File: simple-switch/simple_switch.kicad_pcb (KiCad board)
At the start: 2 copper layers, 28.6 x 27.9 mm, 23 parts, among them J1 CON_TERM_BLK_1X2_TB008A-508-0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, J2 CON_HDR_100MILS_M_TH_2X8, J3 CON_HDR_100MILS_M_TH_1X2, Q1 TRX_PMOS_AOD4189, Q2 TRX_2NPN_BC846S,115

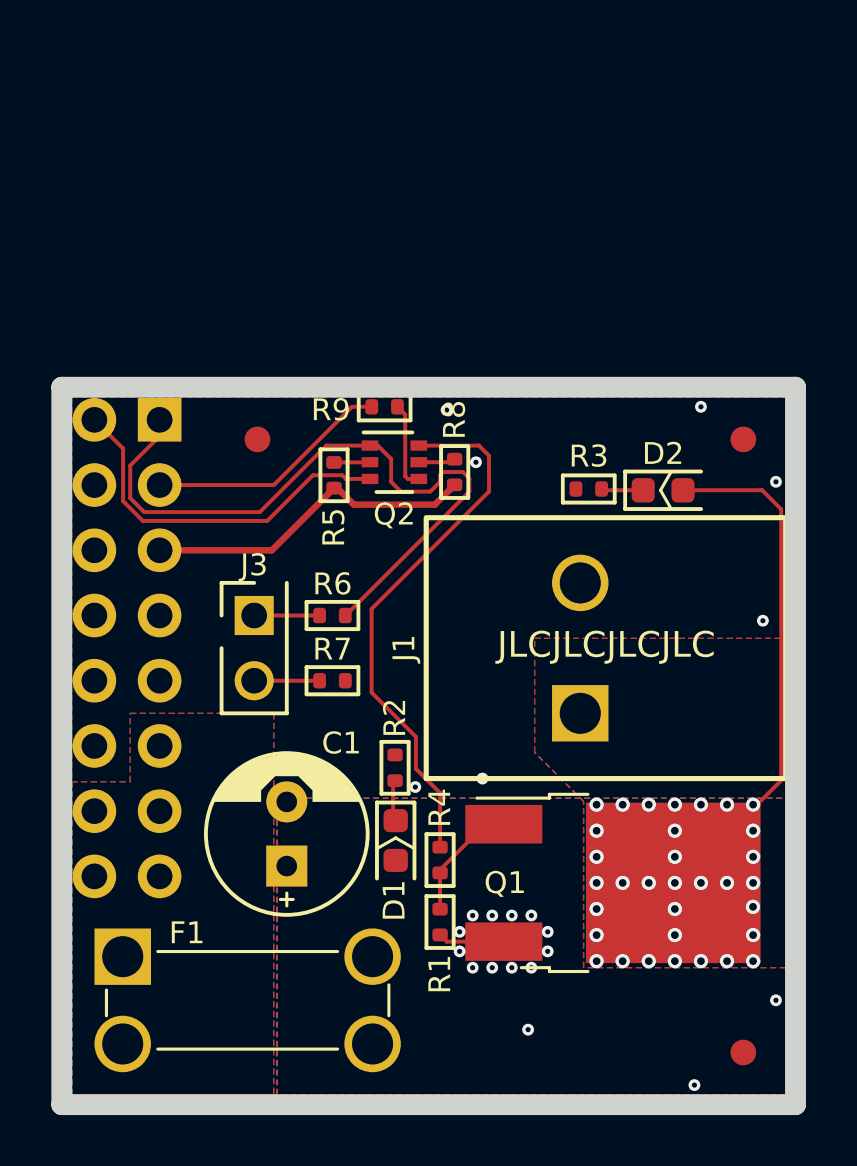
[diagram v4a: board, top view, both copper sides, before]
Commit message: Invert connectors (male/female) Replace TH connectors with SMD ones on mainboard Add 555 timer on simple-switch to generate 60 Hz Add jumper on simple-switch to select AC Add series I2C resistors on mainboard from mikroBUS socket
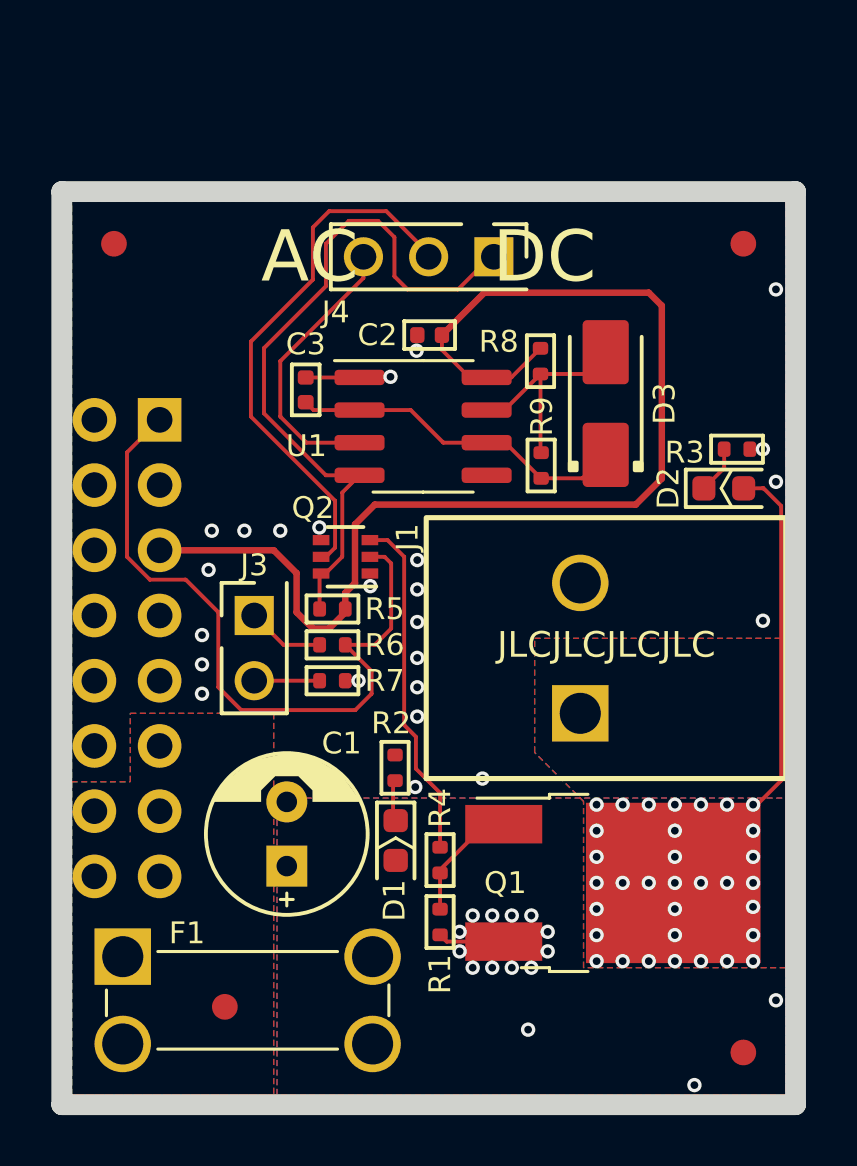
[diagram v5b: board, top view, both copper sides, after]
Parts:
- added C2: CAP_CER_100NF_25V_0402, connaxio-capacitors:CAP_CER_0402_1005M, F.Cu at (128.2, 58.9)
- added C3: CAP_CER_100NF_25V_0402, connaxio-capacitors:CAP_CER_0402_1005M, F.Cu at (123.4, 61.1)
- added D3: DIO_SBD_100V_3A_SMA, connaxio-diodes:DO-214AC_SMA, F.Cu at (135.1, 61.6)
- added F2: FID_1X1, connaxio-mechanical:FID_1X1, F.Cu at (120.3, 85.1)
- added J4: CON_HDR_100MILS_M_TH_1X3, connaxio-connectors:CON_HDR_100MILS_M_TH_1X3, F.Cu at (128.2, 55.9)
- added U1: TIMER_TLC555IDR, connaxio-sop:SOIC-8_3.9x4.9_P1.27, F.Cu at (128.0, 62.5)
- J2: value CON_HDR_100MILS_M_TH_2X8 -> CON_HDR_100MILS_F_TH_2X8; footprint connaxio-connectors:CON_HDR_100MILS_M_TH_2X8 -> connaxio-connectors:CON_HDR_100MILS_F_TH_2X8
- R8: value RES_12.4KΩ_1%_0402 -> RES_100KΩ_1%_0402
- R9: value RES_226Ω_1%_0402 -> RES_169KΩ_1%_0402
- moved F3 9.45 mm to (116.0, 55.4)
- moved F4 7.62 mm to (140.5, 55.4)
- moved R9 6.51 mm to (132.6, 64.0), turned to -90 degrees
- moved R3 5.98 mm to (140.2, 63.4), turned to 0 degrees
- moved R8 5.46 mm to (132.6, 59.9), turned to -90 degrees
- moved R5 5.21 mm to (124.5, 69.6), turned to 180 degrees
- moved G*** 4.57 mm to (132.1, 58.8)
- moved G*** 4.20 mm to (138.8, 64.1)
- moved Q2 4.15 mm to (125.0, 67.6), turned to 180 degrees
- moved D2 2.36 mm to (139.7, 64.9)
- moved R6 1.14 mm to (124.5, 71.0)
- renumbered F2 to F3, F3 to F4, F4 to F5
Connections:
- net Net-(F1-Pad1) renamed /VDR_IN
- J2 pad 2: /~{FAULT} -> unconnected-(J2-Pad2)
- J2 pad 3: /~{CTRLB} -> unconnected-(J2-Pad3)
- Q2 pad 1: /~{CTRLA} -> GND
- Q2 pad 2: Net-(Q2-Pad2) -> /~{CTRLA}
- Q2 pad 3: /~{FAULT} -> /PMOS_GATE
- Q2 pad 4: Net-(Q2-Pad4) -> GND
- Q2 pad 5: Net-(Q2-Pad5) -> /PMOS_CTRL
- Q2 pad 6: /PMOS_CTRL -> /CTRLA_POS
- R4 pad 2: /PMOS_CTRL -> /PMOS_GATE
- R5 pad 2: Net-(Q2-Pad2) -> /CTRLA_POS
- R8 pad 2: Net-(Q2-Pad5) -> Net-(D3-Pad2)
- R9 pad 1: /~{CTRLB} -> Net-(D3-Pad2)
- R9 pad 2: Net-(Q2-Pad4) -> Net-(C3-Pad1)
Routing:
- net +3.3V: track 13.1 -> 47.4 mm
- net /CTRLA_POS: track 0.00 -> 27.8 mm
- net /~{FAULT}: track 14.4 -> 0.00 mm
- net /PMOS_GATE: track 0.00 -> 13.5 mm
- net Net-(C3-Pad1): track 0.00 -> 12.6 mm
- net /AC_OUT: track 0.00 -> 11.2 mm
- net /~{CTRLB}: track 9.53 -> 0.00 mm
- net Net-(D3-Pad2): track 0.00 -> 8.65 mm
- net Net-(Q2-Pad4): track 3.40 -> 0.00 mm
- net /VOUT: track 20.5 -> 18.3 mm
- net GND: track 0.00 -> 2.10 mm, vias 7 -> 24
- net Net-(Q2-Pad5): track 1.45 -> 0.00 mm
- net Net-(Q2-Pad2): track 1.41 -> 0.00 mm
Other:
- board size 28.6 x 27.9 mm -> 28.6 x 35.6 mm
- board text added: "AC DC"

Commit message: Add flyback diode to simple-switch
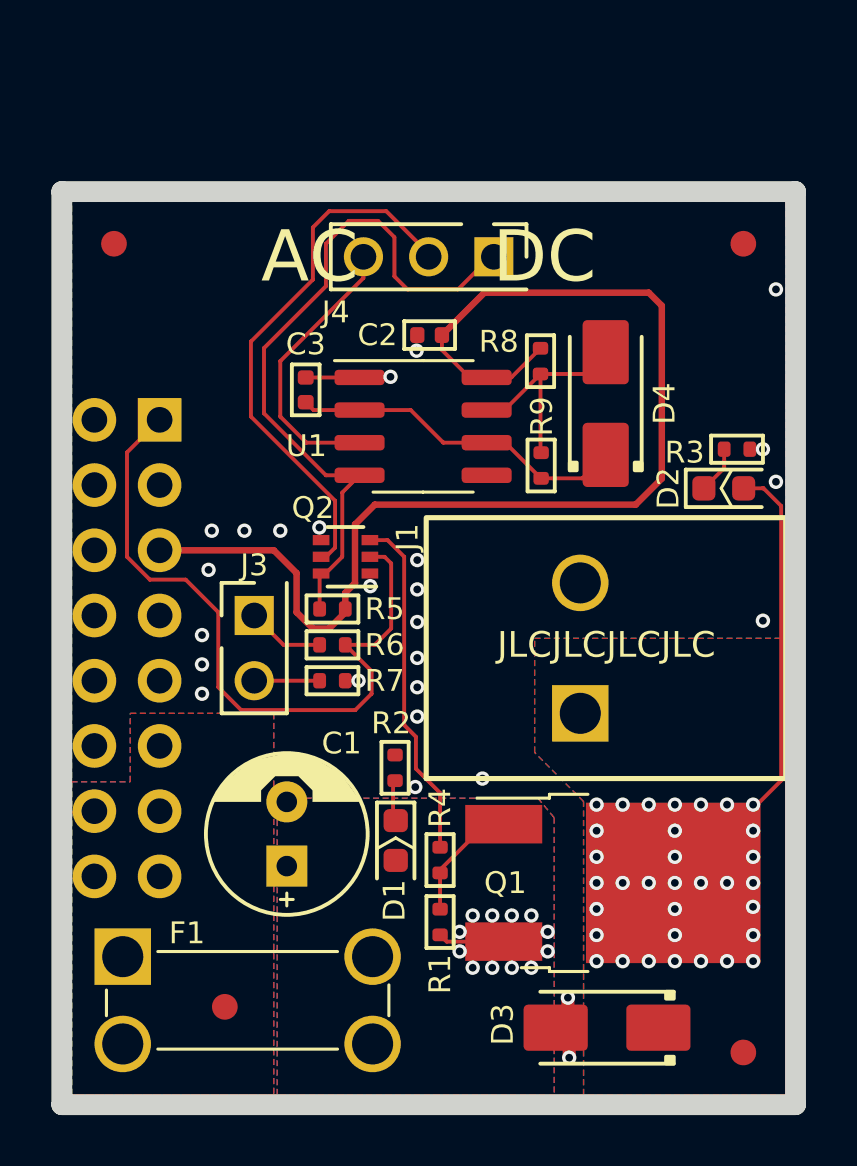
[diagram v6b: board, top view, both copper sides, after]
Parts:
- added D3: DIO_SBD_100V_3A_SMA, connaxio-diodes:DO-214AC_SMA, F.Cu at (135.2, 85.9)
- renumbered D3 to D4
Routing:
- net GND: track 2.10 -> 4.85 mm, vias 24 -> 26
- net Vdrive: vias 15 -> 12
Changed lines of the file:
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@@
   (net 9 "Net-(J3-Pad1)")
   (net 10 "Net-(J3-Pad2)")
-  (net 11 "Net-(D3-Pad2)")
+  (net 11 "Net-(D4-Pad2)")
   (net 12 "unconnected-(J2-Pad4)")
   (net 13 "unconnected-(J2-Pad2)")
@@
     )
   )
+  (footprint "connaxio-diodes:DO-214AC_SMA" (layer "F.Cu")
+    (at 135.1534 85.9028 180)
+    (descr "Diode SMA (DO-214AC)")
+    (tags "Diode SMA (DO-214AC)")
+    (property "Current" "3A")
+    (property "Manufacturer" "Micro Commercial Co")
+    (property "Manufacturer Part Number" "SL310A-TP")
+    (property "Package" "SMA")
+    (property "Polarized" "Yes")
+    (property "Sheetfile" "simple_switch.kicad_sch")
+    (property "Sheetname" "")
+    (property "Temperature" "-55°C to +150°C")
+    (property "Tolerance" "60A")
+    (property "Voltage" "100V")
+    (solder_mask_margin 0.05)
+    (attr smd)
+    (fp_text reference "D3" (at 4.064 0.127 90) (layer "F.SilkS")
+      (effects (font (size 0.85 0.85) (thickness 0.15)))
+    )
+    (fp_text value "DIO_SBD_100V_3A_SMA" (at 0 2.6) (layer "F.Fab")
+      (effects (font (size 1 1) (thickness 0.15)))
+    )
+    (fp_text user "${REFERENCE}" (at 0 -2.5) (layer "F.Fab")
+      (effects (font (size 1 1) (thickness 0.15)))
+    )
+    (fp_line (start -2.6 -1.4) (end 2.6 -1.4) (layer "F.SilkS") (width 0.15))
+    (fp_line (start -2.6 1.4) (end 2.6 1.4) (layer "F.SilkS") (width 0.15))
+    (fp_poly (pts
+        (xy -2.3 -1.13)
+        (xy -2.6 -1.13)
+        (xy -2.6 -1.4)
+        (xy -2.3 -1.4)
+      ) (layer "F.SilkS") (width 0.15) (fill solid))
+    (fp_poly (pts
+        (xy -2.3 1.4)
+        (xy -2.6 1.4)
+        (xy -2.6 1.13)
+        (xy -2.3 1.13)
+      ) (layer "F.SilkS") (width 0.15) (fill solid))
+    (fp_line (start -3.5 -1.75) (end 3.5 -1.75) (layer "F.CrtYd") (width 0.05))
+    (fp_line (start -3.5 1.75) (end -3.5 -1.75) (layer "F.CrtYd") (width 0.05))
+    (fp_line (start 3.5 -1.75) (end 3.5 1.75) (layer "F.CrtYd") (width 0.05))
+    (fp_line (start 3.5 1.75) (end -3.5 1.75) (layer "F.CrtYd") (width 0.05))
+    (fp_line (start -2.3 1.5) (end -2.3 -1.5) (layer "F.Fab") (width 0.1))
+    (fp_line (start -0.64944 0.00102) (end 0.50118 -0.79908) (layer "F.Fab") (width 0.1))
+    (fp_line (start -0.64944 -0.79908) (end -0.64944 0.80112) (layer "F.Fab") (width 0.1))
+    (fp_line (start -0.64944 0.00102) (end -1.55114 0.00102) (layer "F.Fab") (width 0.1))
+    (fp_line (start 2.3 1.5) (end -2.3 1.5) (layer "F.Fab") (width 0.1))
+    (fp_line (start -0.64944 0.00102) (end 0.50118 0.75032) (layer "F.Fab") (width 0.1))
+    (fp_line (start 0.50118 0.00102) (end 1.4994 0.00102) (layer "F.Fab") (width 0.1))
+    (fp_line (start 0.50118 0.75032) (end 0.50118 -0.79908) (layer "F.Fab") (width 0.1))
+    (fp_line (start 2.3 -1.5) (end -2.3 -1.5) (layer "F.Fab") (width 0.1))
+    (fp_line (start 2.3 -1.5) (end 2.3 1.5) (layer "F.Fab") (width 0.1))
+    (pad "1" smd roundrect (at -2 0 180) (size 2.5 1.8) (layers "F.Cu" "F.Paste" "F.Mask") (roundrect_rratio 0.1)
+      (net 18 "/VOUT") (pinfunction "K") (pintype "passive"))
+    (pad "2" smd roundrect (at 2 0 180) (size 2.5 1.8) (layers "F.Cu" "F.Paste" "F.Mask") (roundrect_rratio 0.1)
+      (net 2 "GND") (pinfunction "A") (pintype "passive"))
+    (model ":CONNAXIO_KICAD_LIB_DIR:connaxio-diodes.3dshapes/DO-214AC_SMA.wrl"
+      (offset (xyz 0 0 0))
+      (scale (xyz 1 1 1))
+      (rotate (xyz 0 0 0))
+    )
+  )
   (footprint "connaxio-diodes:LED_0603_1608M" (layer "F.Cu")
     (at 126.9238 78.613 -90)
@@
       (net 1 "+3.3V") (pinfunction "1") (pintype "passive"))
     (pad "2" smd roundrect (at 0.5 0 270) (size 0.5 0.6) (layers "F.Cu" "F.Paste" "F.Mask") (roundrect_rratio 0.25)
-      (net 11 "Net-(D3-Pad2)") (pinfunction "2") (pintype "passive"))
+      (net 11 "Net-(D4-Pad2)") (pinfunction "2") (pintype "passive"))
     (model ":CONNAXIO_KICAD_LIB_DIR:connaxio-resistors.3dshapes/RES_0402_1005M.wrl"
       (offset (xyz 0 0 0))
@@
       (net 7 "Net-(C3-Pad1)") (pinfunction "THRES") (pintype "input"))
     (pad "7" smd roundrect (at 2.475 -0.635) (size 1.95 0.6) (layers "F.Cu" "F.Paste" "F.Mask") (roundrect_rratio 0.25)
-      (net 11 "Net-(D3-Pad2)") (pinfunction "DISCH") (pintype "output"))
+      (net 11 "Net-(D4-Pad2)") (pinfunction "DISCH") (pintype "output"))
     (pad "8" smd roundrect (at 2.475 -1.905) (size 1.95 0.6) (layers "F.Cu" "F.Paste" "F.Mask") (roundrect_rratio 0.25)
       (net 1 "+3.3V") (pinfunction "VDD") (pintype "power_in"))
@@
     (fp_line (start -0.5 0.25) (end -0.5 -0.25) (layer "F.Fab") (width 0.1))
     (pad "1" smd roundrect (at -0.5 0 270) (size 0.5 0.6) (layers "F.Cu" "F.Paste" "F.Mask") (roundrect_rratio 0.25)
-      (net 11 "Net-(D3-Pad2)") (pinfunction "1") (pintype "passive"))
+      (net 11 "Net-(D4-Pad2)") (pinfunction "1") (pintype "passive"))
     (pad "2" smd roundrect (at 0.5 0 270) (size 0.5 0.6) (layers "F.Cu" "F.Paste" "F.Mask") (roundrect_rratio 0.25)
       (net 7 "Net-(C3-Pad1)") (pinfunction "2") (pintype "passive"))
@@
     (solder_mask_margin 0.05)
     (attr smd)
-    (fp_text reference "D3" (at 0 2.286 90) (layer "F.SilkS")
+    (fp_text reference "D4" (at 0 2.286 90) (layer "F.SilkS")
       (effects (font (size 0.85 0.85) (thickness 0.15)))
     )
@@
       (net 7 "Net-(C3-Pad1)") (pinfunction "K") (pintype "passive"))
     (pad "2" smd roundrect (at 2 0 90) (size 2.5 1.8) (layers "F.Cu" "F.Paste" "F.Mask") (roundrect_rratio 0.1)
-      (net 11 "Net-(D3-Pad2)") (pinfunction "A") (pintype "passive"))
+      (net 11 "Net-(D4-Pad2)") (pinfunction "A") (pintype "passive"))
     (model ":CONNAXIO_KICAD_LIB_DIR:connaxio-diodes.3dshapes/DO-214AC_SMA.wrl"
       (offset (xyz 0 0 0))
@@
   (segment (start 123.698 70.358) (end 123.063 69.723) (width 0.254) (layer "F.Cu") (net 1))
   (segment (start 125.513 60.5816) (end 125.5156 60.579) (width 0.1524) (layer "F.Cu") (net 2))
+  (segment (start 133.6802 86.4296) (end 133.1534 85.9028) (width 0.1524) (layer "F.Cu") (net 2))
+  (segment (start 133.6294 84.7344) (end 133.6294 85.4268) (width 0.508) (layer "F.Cu") (net 2))
   (segment (start 123.4186 60.5816) (end 125.513 60.5816) (width 0.1524) (layer "F.Cu") (net 2))
+  (segment (start 133.6802 87.0712) (end 133.6802 86.4296) (width 0.508) (layer "F.Cu") (net 2))
+  (segment (start 133.6294 85.4268) (end 133.1534 85.9028) (width 0.1524) (layer "F.Cu") (net 2))
   (via (at 141.224 63.373) (size 0.56) (drill 0.3) (layers "F.Cu" "B.Cu") (free) (net 2))
   (via (at 119.761 66.548) (size 0.56) (drill 0.3) (layers "F.Cu" "B.Cu") (free) (net 2))
@@
   (via (at 141.224 70.0532) (size 0.56) (drill 0.3) (layers "F.Cu" "B.Cu") (free) (net 2))
   (via (at 141.732 57.15) (size 0.56) (drill 0.3) (layers "F.Cu" "B.Cu") (free) (net 2))
+  (via (at 133.6294 84.7344) (size 0.56) (drill 0.3) (layers "F.Cu" "B.Cu") (free) (net 2))
   (via (at 119.38 70.612) (size 0.56) (drill 0.3) (layers "F.Cu" "B.Cu") (free) (net 2))
   (via (at 130.302 76.2) (size 0.56) (drill 0.3) (layers "F.Cu" "B.Cu") (free) (net 2))
@@
   (via (at 127.6858 76.5302) (size 0.56) (drill 0.3) (layers "F.Cu" "B.Cu") (free) (net 2))
   (via (at 119.38 72.898) (size 0.56) (drill 0.3) (layers "F.Cu" "B.Cu") (free) (net 2))
+  (via (at 133.6802 87.0712) (size 0.56) (drill 0.3) (layers "F.Cu" "B.Cu") (free) (net 2))
   (via (at 125.9332 68.707) (size 0.56) (drill 0.3) (layers "F.Cu" "B.Cu") (free) (net 2))
   (via (at 127.762 70.104) (size 0.56) (drill 0.3) (layers "F.Cu" "B.Cu") (free) (net 2))
@@
   (via (at 131.445 83.566) (size 0.56) (drill 0.3) (layers "F.Cu" "B.Cu") (free) (net 5))
   (via (at 130.683 83.566) (size 0.56) (drill 0.3) (layers "F.Cu" "B.Cu") (free) (net 5))
-  (via (at 138.557 88.138) (size 0.56) (drill 0.3) (layers "F.Cu" "B.Cu") (free) (net 5))
   (via (at 131.445 81.534) (size 0.56) (drill 0.3) (layers "F.Cu" "B.Cu") (free) (net 5))
-  (via (at 132.08 85.979) (size 0.56) (drill 0.3) (layers "F.Cu" "B.Cu") (free) (net 5))
   (via (at 132.207 83.566) (size 0.56) (drill 0.3) (layers "F.Cu" "B.Cu") (free) (net 5))
-  (via (at 141.732 84.836) (size 0.56) (drill 0.3) (layers "F.Cu" "B.Cu") (free) (net 5))
   (segment (start 125.984 72.017) (end 124.96 70.993) (width 0.1524) (layer "F.Cu") (net 6))
   (segment (start 126.111 70.993) (end 124.96 70.993) (width 0.1524) (layer "F.Cu") (net 6))
@@
     (polygon
       (pts
-        (xy 142.113 88.519)
+        (xy 133.096 77.724)
+        (xy 133.096 88.519)
         (xy 122.301 88.519)
         (xy 122.301 76.962)
-        (xy 142.113 76.962)
+        (xy 132.461 76.962)
       )
     )
@@
     (polygon
       (pts
-        (xy 142.113 83.566)
-        (xy 134.239 83.566)
+        (xy 142.113 88.519)
+        (xy 134.239 88.519)
         (xy 134.239 77.089)
         (xy 132.334 75.184)
